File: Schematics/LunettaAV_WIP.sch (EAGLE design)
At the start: 50 parts, among them IC1 TLC339P, IC2 7805T, IC3 4046N, IC4 4040N, IC5 4017N, IC6 4051N, IC7 4094N, IC8 4046N, IC9 40106N, U1 LM358

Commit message: schematic updates
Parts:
- added C2: .1uF, capacitor-wima:C2.5/2
- added R23: LDR, rcl:R-EU_0204/2V
- added VR4: 100K, MusicThingModular:9MM_SNAP-IN_POT_
- R21: value (none) -> 10K
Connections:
- removed net MELODYBUFF: D1.C, VR3.E
- new net N$10: IC9B.O, IC9C.I
- new net N$12: C2.1, IC9A.I, R23.2, VR4.S
- new net N$9: IC9A.O, IC9B.I, R23.1, VR4.A
- net AUDIORATE: now also IC9C.O
- net GND: now also C2.2, IC9D.I, IC9E.I, IC9F.I
- net MELODYOUT: now also D1.C, VR3.E
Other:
- moved on the sheet: IC9A, IC9B, IC9C, IC9D, IC9E, IC9F, IC9P, JP6

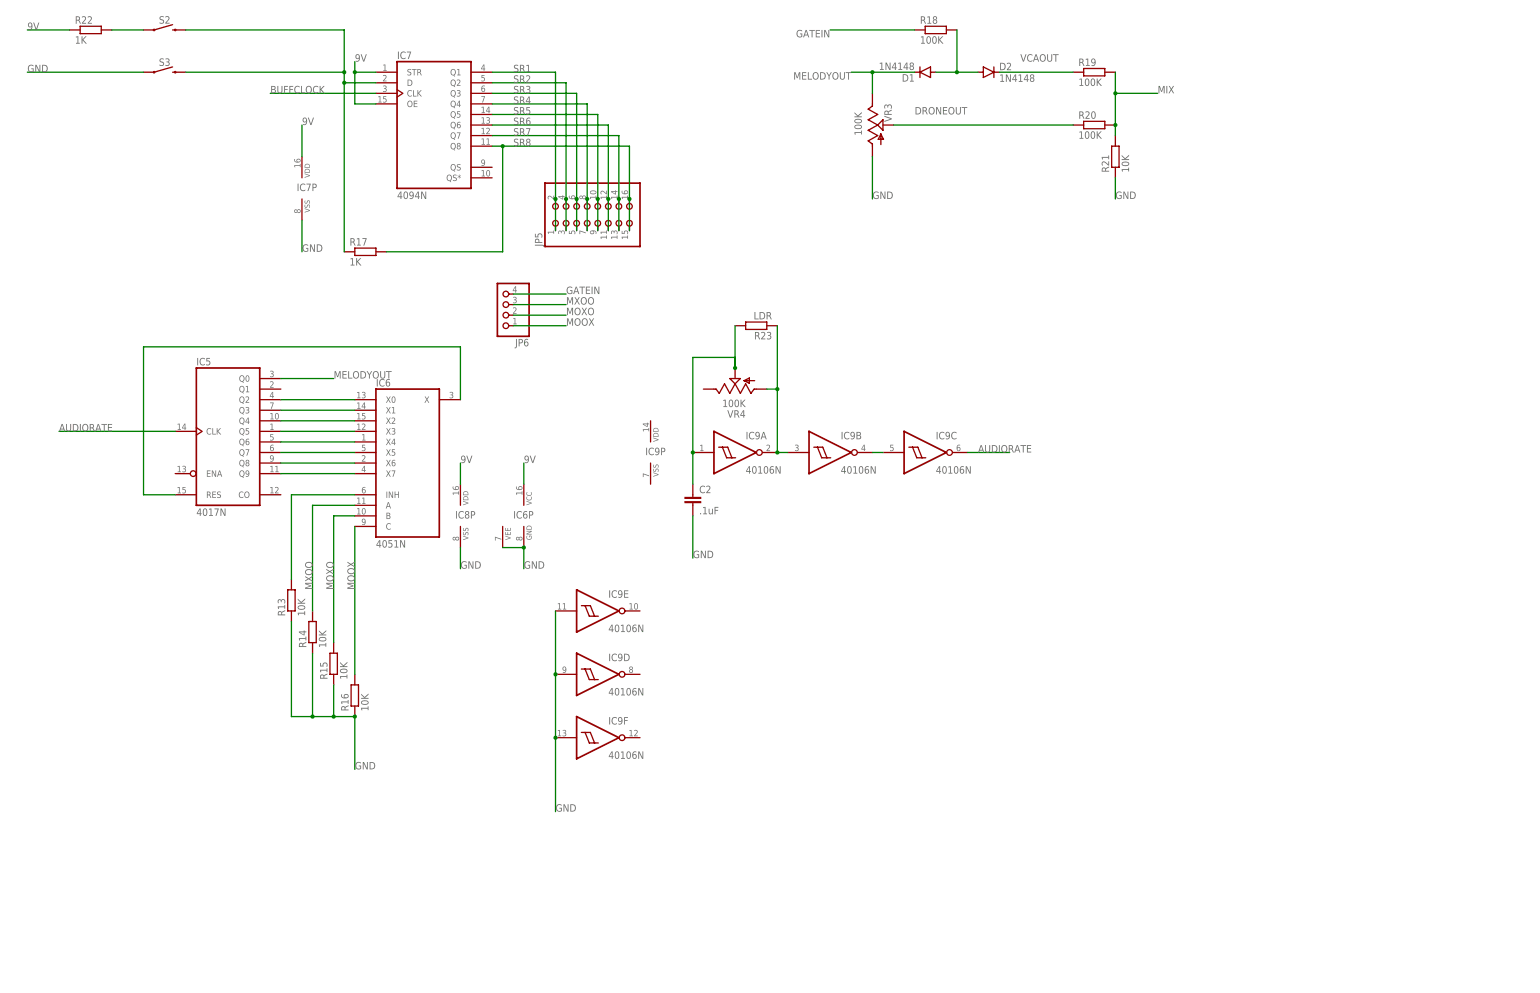
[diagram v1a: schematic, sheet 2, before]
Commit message: more visuals and functions updated
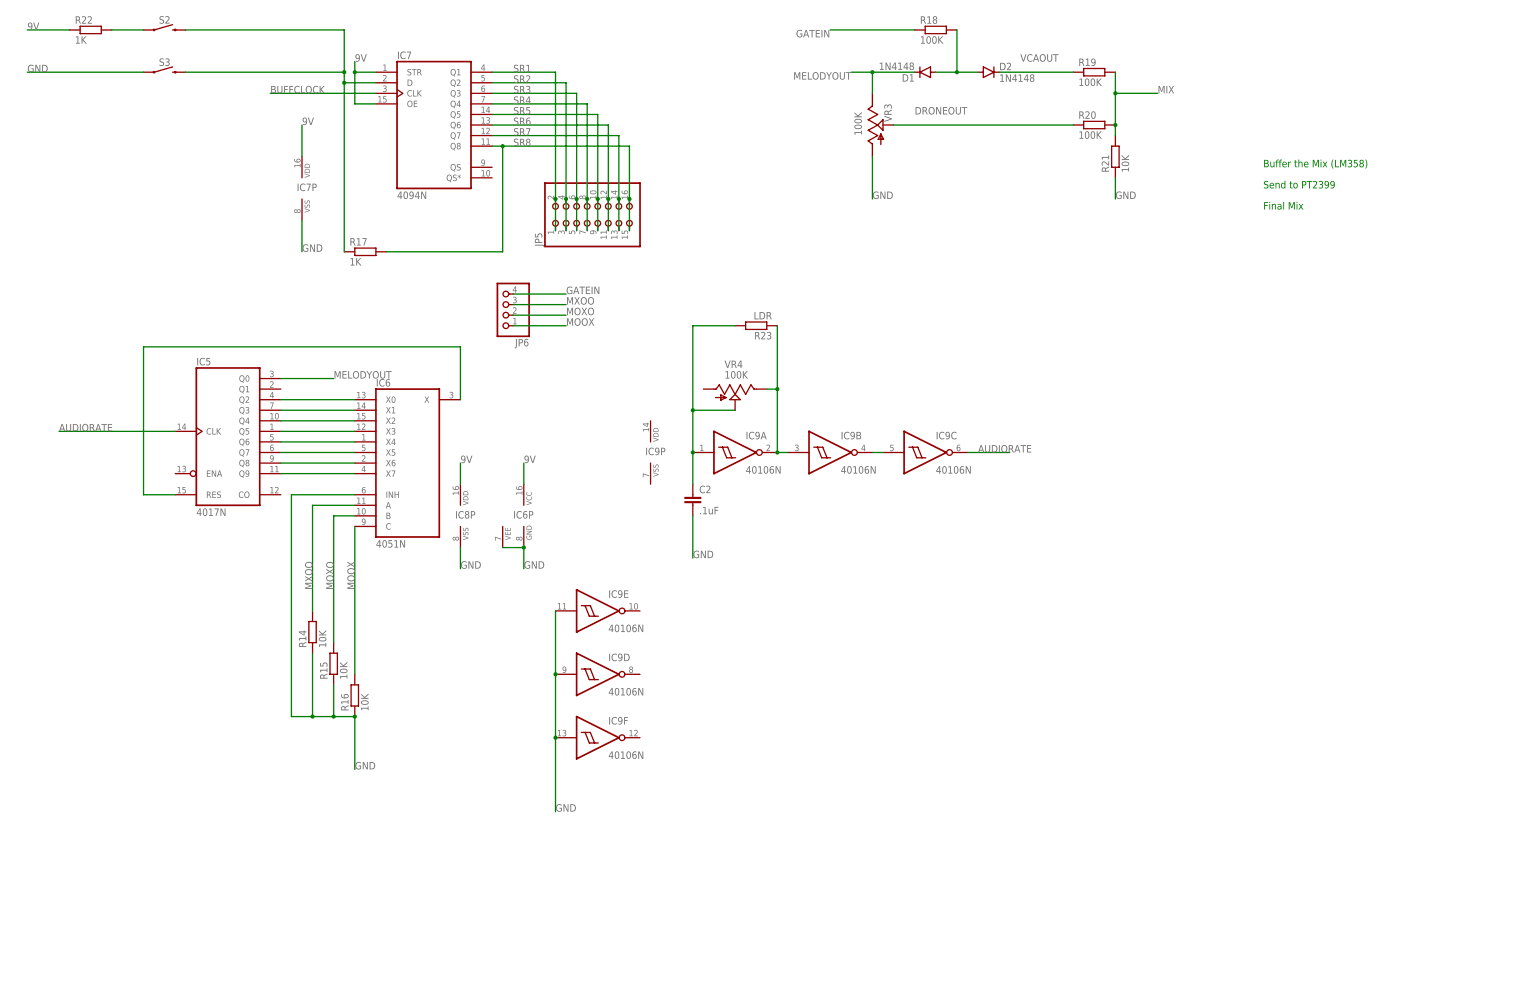
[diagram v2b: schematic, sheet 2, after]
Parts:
- removed R13: 10K, MusicThingModular:RESISTOR7MM
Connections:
- removed net N$11 (its old number): IC6A.INH, R13.2
- net GND: now also IC6A.INH; no longer R13.1
- net N$9: now also VR4.E; no longer VR4.A
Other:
- note added: "Buffer the Mix (LM358)"
- note added: "Final Mix"
- note added: "Send to PT2399"
- moved on the sheet: VR4
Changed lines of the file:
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@@
 <part name="R21" library="MusicThingModular" deviceset="RESISTOR" device="7MM" value="10K"/>
 <part name="R17" library="MusicThingModular" deviceset="RESISTOR" device="7MM" value="1K"/>
-<part name="R13" library="MusicThingModular" deviceset="RESISTOR" device="7MM" value="10K"/>
 <part name="R14" library="MusicThingModular" deviceset="RESISTOR" device="7MM" value="10K"/>
 <part name="R15" library="MusicThingModular" deviceset="RESISTOR" device="7MM" value="10K"/>
@@
 <sheet>
 <plain>
+<text x="314.96" y="-116.84" size="1.778" layer="91">Buffer the Mix (LM358)</text>
+<text x="314.96" y="-121.92" size="1.778" layer="91">Send to PT2399</text>
+<text x="314.96" y="-127" size="1.778" layer="91">Final Mix</text>
 </plain>
 <instances>
@@
 <attribute name="VALUE" x="95.25" y="-140.462" size="1.778" layer="96"/>
 </instance>
-<instance part="R13" gate="G$1" x="81.28" y="-220.98" smashed="yes" rot="R90">
-<attribute name="NAME" x="79.7814" y="-224.79" size="1.778" layer="95" rot="R90"/>
-<attribute name="VALUE" x="84.582" y="-224.79" size="1.778" layer="96" rot="R90"/>
-</instance>
 <instance part="R14" gate="G$1" x="86.36" y="-228.6" smashed="yes" rot="R90">
 <attribute name="NAME" x="84.8614" y="-232.41" size="1.778" layer="95" rot="R90"/>
@@
 <attribute name="VALUE" x="29.21" y="-87.122" size="1.778" layer="96"/>
 </instance>
-<instance part="VR4" gate="G$1" x="187.96" y="-170.18" smashed="yes" rot="R90">
-<attribute name="NAME" x="190.5" y="-175.26" size="1.778" layer="95" rot="R180"/>
-<attribute name="VALUE" x="190.5" y="-172.72" size="1.778" layer="96" rot="R180"/>
+<instance part="VR4" gate="G$1" x="187.96" y="-170.18" smashed="yes" rot="R270">
+<attribute name="NAME" x="185.42" y="-165.1" size="1.778" layer="95"/>
+<attribute name="VALUE" x="185.42" y="-167.64" size="1.778" layer="96"/>
 </instance>
 <instance part="C2" gate="G$1" x="177.8" y="-195.58" smashed="yes">
@@
 </segment>
 <segment>
-<pinref part="R13" gate="G$1" pin="1"/>
-<wire x1="81.28" y1="-226.06" x2="81.28" y2="-248.92" width="0.1524" layer="91"/>
 <pinref part="R16" gate="G$1" pin="1"/>
 <wire x1="81.28" y1="-248.92" x2="86.36" y2="-248.92" width="0.1524" layer="91"/>
@@
 <junction x="86.36" y="-248.92"/>
 <label x="96.52" y="-261.62" size="1.778" layer="95"/>
+<pinref part="IC6" gate="A" pin="INH"/>
+<wire x1="96.52" y1="-195.58" x2="81.28" y2="-195.58" width="0.1524" layer="91"/>
+<wire x1="81.28" y1="-195.58" x2="81.28" y2="-248.92" width="0.1524" layer="91"/>
 </segment>
 <segment>
@@
 </segment>
 </net>
-<net name="N$11" class="0">
-<segment>
-<pinref part="IC6" gate="A" pin="INH"/>
-<pinref part="R13" gate="G$1" pin="2"/>
-<wire x1="96.52" y1="-195.58" x2="81.28" y2="-195.58" width="0.1524" layer="91"/>
-<wire x1="81.28" y1="-195.58" x2="81.28" y2="-215.9" width="0.1524" layer="91"/>
-</segment>
-</net>
 <net name="N$8" class="0">
 <segment>
@@
 <pinref part="IC9" gate="B" pin="I"/>
 <wire x1="198.12" y1="-185.42" x2="200.66" y2="-185.42" width="0.1524" layer="91"/>
-<wire x1="198.12" y1="-185.42" x2="198.12" y2="-170.18" width="0.1524" layer="91"/>
 <junction x="198.12" y="-185.42"/>
-<pinref part="VR4" gate="G$1" pin="A"/>
-<wire x1="198.12" y1="-170.18" x2="195.58" y2="-170.18" width="0.1524" layer="91"/>
 <pinref part="R23" gate="G$1" pin="1"/>
 <wire x1="198.12" y1="-154.94" x2="198.12" y2="-170.18" width="0.1524" layer="91"/>
+<pinref part="VR4" gate="G$1" pin="E"/>
+<wire x1="198.12" y1="-170.18" x2="198.12" y2="-185.42" width="0.1524" layer="91"/>
+<wire x1="195.58" y1="-170.18" x2="198.12" y2="-170.18" width="0.1524" layer="91"/>
 <junction x="198.12" y="-170.18"/>
 </segment>
@@
 </segment>
 </net>
-<net name="N$12" class="0">
-<segment>
+<net name="N$11" class="0">
+<segment>
+<pinref part="C2" gate="G$1" pin="1"/>
 <pinref part="IC9" gate="A" pin="I"/>
 <wire x1="177.8" y1="-185.42" x2="177.8" y2="-193.04" width="0.1524" layer="91"/>
-<pinref part="C2" gate="G$1" pin="1"/>
 <pinref part="VR4" gate="G$1" pin="S"/>
-<wire x1="187.96" y1="-165.1" x2="187.96" y2="-162.56" width="0.1524" layer="91"/>
-<wire x1="187.96" y1="-162.56" x2="177.8" y2="-162.56" width="0.1524" layer="91"/>
-<wire x1="177.8" y1="-162.56" x2="177.8" y2="-185.42" width="0.1524" layer="91"/>
+<wire x1="187.96" y1="-175.26" x2="177.8" y2="-175.26" width="0.1524" layer="91"/>
+<wire x1="177.8" y1="-175.26" x2="177.8" y2="-185.42" width="0.1524" layer="91"/>
 <junction x="177.8" y="-185.42"/>
 <pinref part="R23" gate="G$1" pin="2"/>
-<wire x1="187.96" y1="-154.94" x2="187.96" y2="-165.1" width="0.1524" layer="91"/>
-<junction x="187.96" y="-165.1"/>
-</segment>
-</net>
+<wire x1="187.96" y1="-154.94" x2="177.8" y2="-154.94" width="0.1524" layer="91"/>
+<wire x1="177.8" y1="-154.94" x2="177.8" y2="-175.26" width="0.1524" layer="91"/>
+<junction x="177.8" y="-175.26"/>
+</segment>
+</net>

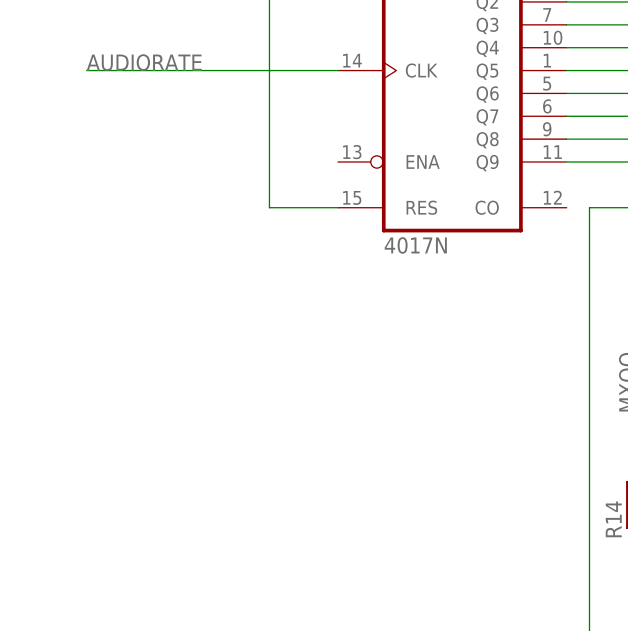
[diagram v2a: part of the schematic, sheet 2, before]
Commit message: fix 4017 schematics
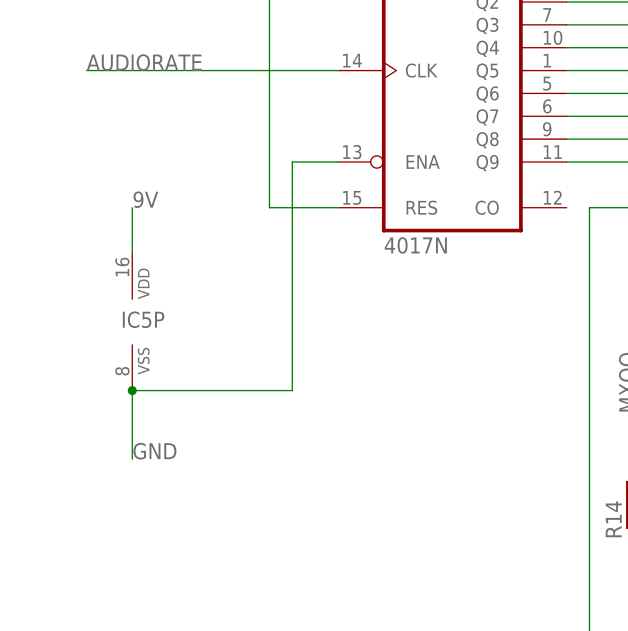
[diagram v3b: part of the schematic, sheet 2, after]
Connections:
- net 9V: now also IC5P.VDD
- net GND: now also IC5A.ENA, IC5P.VSS
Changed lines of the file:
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@@
 <attribute name="VALUE" x="196.85" y="-151.638" size="1.778" layer="96" rot="R180"/>
+</instance>
+<instance part="IC5" gate="P" x="30.48" y="-208.28" smashed="yes">
+<attribute name="NAME" x="29.21" y="-208.915" size="1.778" layer="95"/>
 </instance>
 </instances>
@@
 <wire x1="27.94" y1="-83.82" x2="17.78" y2="-83.82" width="0.1524" layer="91"/>
 <label x="17.78" y="-83.82" size="1.778" layer="95"/>
+</segment>
+<segment>
+<pinref part="IC5" gate="P" pin="VDD"/>
+<wire x1="30.48" y1="-200.66" x2="30.48" y2="-195.58" width="0.1524" layer="91"/>
+<label x="30.48" y="-195.58" size="1.778" layer="95"/>
 </segment>
 </net>
@@
 <label x="144.78" y="-271.78" size="1.778" layer="95"/>
 </segment>
+<segment>
+<pinref part="IC5" gate="P" pin="VSS"/>
+<wire x1="30.48" y1="-215.9" x2="30.48" y2="-223.52" width="0.1524" layer="91"/>
+<label x="30.48" y="-223.52" size="1.778" layer="95"/>
+<pinref part="IC5" gate="A" pin="ENA"/>
+<wire x1="53.34" y1="-190.5" x2="48.26" y2="-190.5" width="0.1524" layer="91"/>
+<wire x1="48.26" y1="-190.5" x2="48.26" y2="-215.9" width="0.1524" layer="91"/>
+<wire x1="48.26" y1="-215.9" x2="30.48" y2="-215.9" width="0.1524" layer="91"/>
+<junction x="30.48" y="-215.9"/>
+</segment>
 </net>

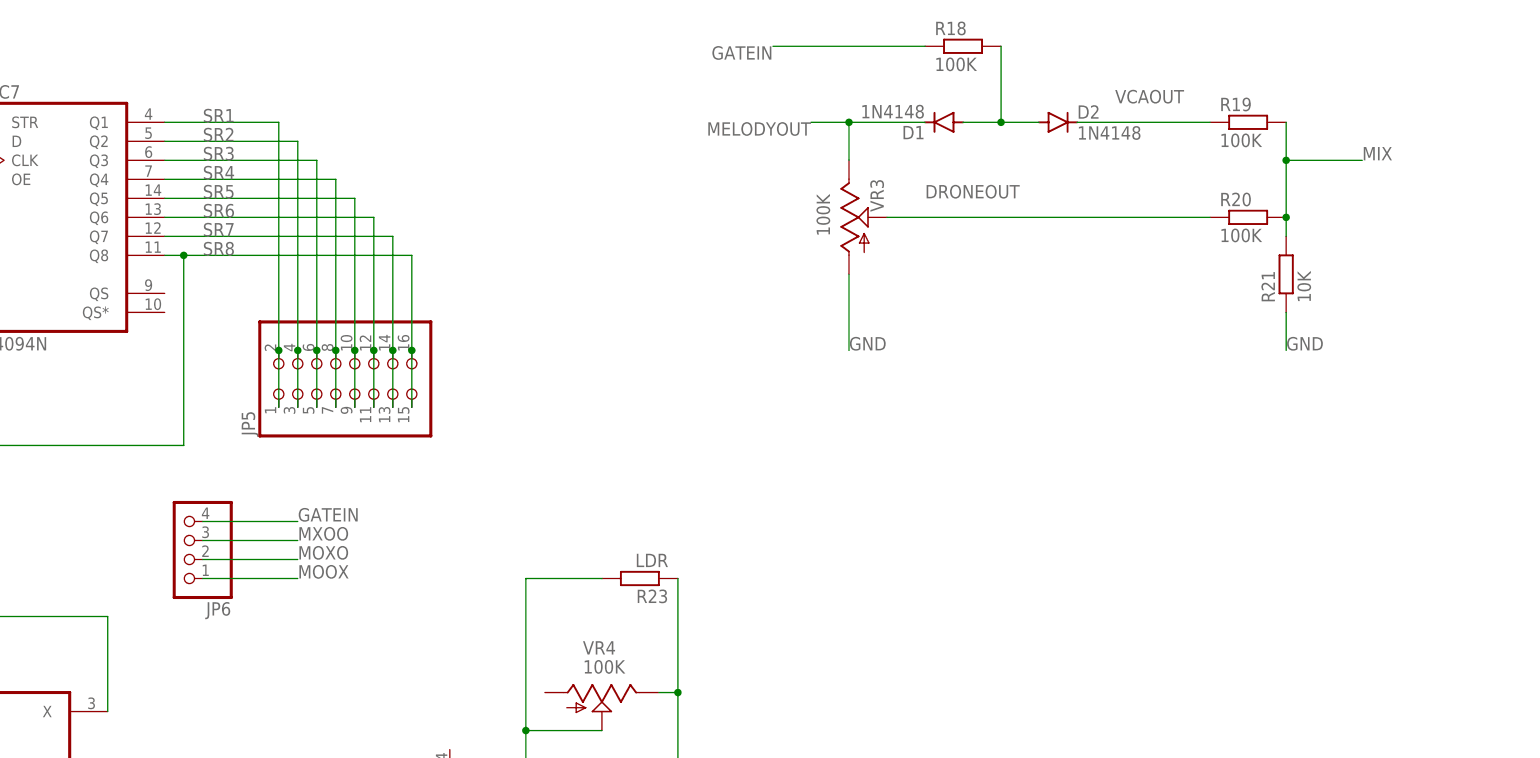
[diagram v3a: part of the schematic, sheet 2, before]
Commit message: change melody out config and buffer the out for later stage
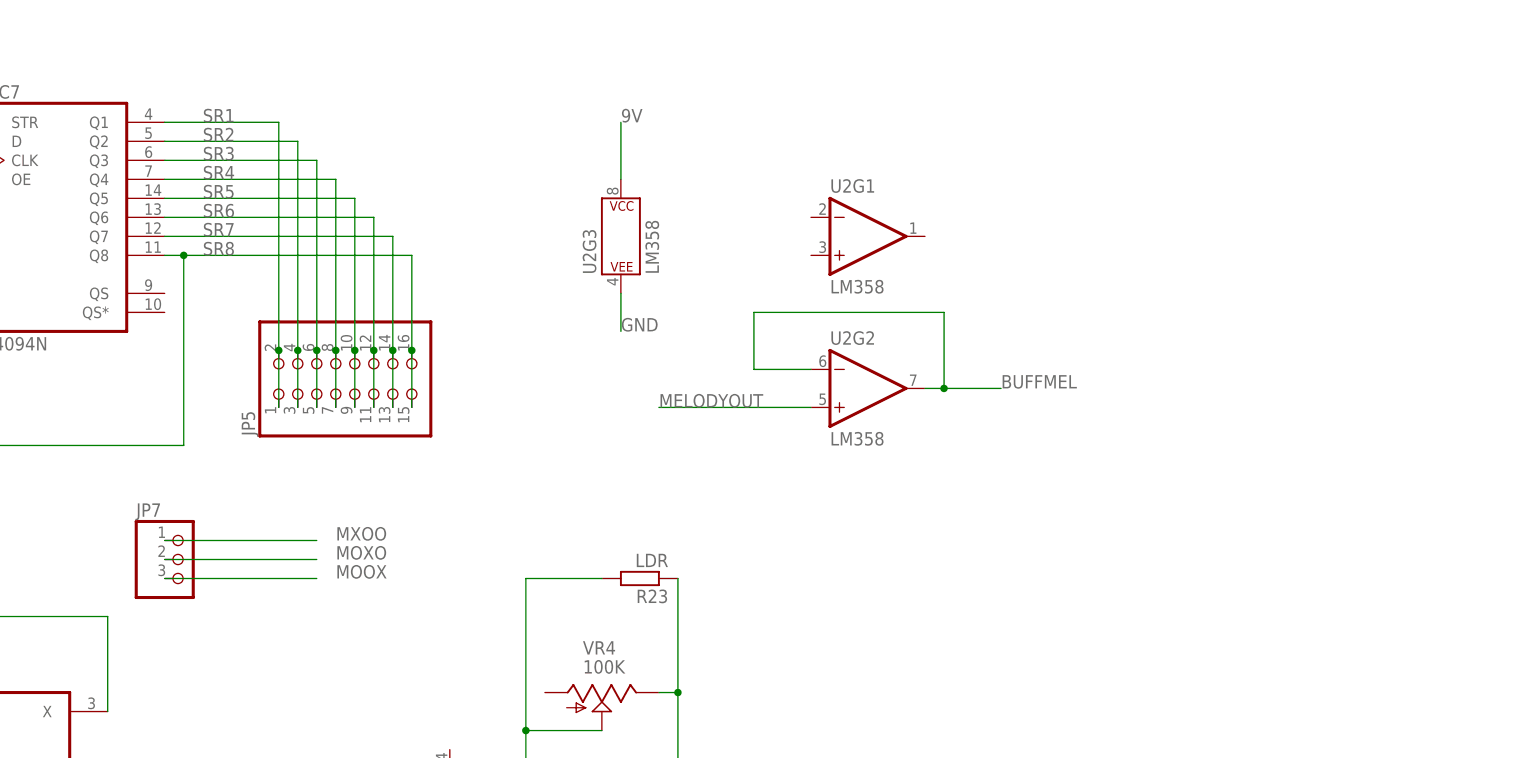
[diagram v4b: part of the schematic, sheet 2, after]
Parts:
- removed D1, D2: 1N4148, diode:1N4148DO35-10
- removed JP6: (no value), pinhead:PINHD-1X4
- removed R18, R19, R20: 100K, MusicThingModular:RESISTOR7MM
- removed R21: 10K, MusicThingModular:RESISTOR7MM
- removed VR3: 100K, MusicThingModular:9MM_SNAP-IN_POT_
- added JP7: (no value), pinhead:PINHD-1X3
- added U2: LM358, SparkFun-IC-Amplifiers:LM358
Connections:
- removed net DRONEOUT: R20.1, VR3.S
- removed net GATEIN: JP6.4, R18.1
- removed net MIX: R19.2, R20.2, R21.2
- removed net N$7: D1.A, D2.A, R18.2
- removed net VCAOUT: D2.C, R19.1
- new net BUFFMEL: U2G2.-IN, U2G2.OUT
- net 9V: now also U2G3.P$V+
- net GND: now also U2G3.P$V-; no longer R21.1, VR3.A
- net MELODYOUT: now also U2G2.+IN; no longer D1.C, VR3.E
- net MOOX: now also JP7.3; no longer JP6.1
- net MOXO: now also JP7.2; no longer JP6.2
- net MXOO: now also JP7.1; no longer JP6.3

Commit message: PT2399 init + screen changed
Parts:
- removed DISP$1, DISP$2: DISPLAY-OLED-128X64-I2C, diy-modules:DISPLAY-OLED-128X64-I2C
- added C10, C8, C9: 10uF, SparkFun-Capacitors:10UF-POLAR-RADIAL-2.5MM-25V-20%
- added C11: 47uF, SparkFun-Capacitors:10UF-POLAR-RADIAL-2.5MM-25V-20%
- added C12, C13, C4, C5, C6, C7: 0.1uF, SparkFun-Capacitors:0.1UF-KIT-EZ-50V-20%
- added C3: 100uF, SparkFun-Capacitors:100UF-POLAR-RADIAL-2.5MM-25V-20%
- added DD1: PT2399, ic-princeton-technologies:PT2399
- added IC10: (no value), v-reg:78XXS
- added J1: POWER_JACKPOWER_JACK_SLOT, SparkFun-Connectors:POWER_JACKPOWER_JACK_SLOT
- added R13: (no value), MusicThingModular:RESISTOR7MM
- added R18: 10k, MusicThingModular:RESISTOR7MM
- added R19: 100k, MusicThingModular:RESISTOR7MM
- added U$1, U$2: OLED_0.96_I2C, tft_1_8_1_44_oled_0_96:OLED_0.96_I2C
- added VR3: (no value), MusicThingModular:9MM_SNAP-IN_POT_
- C1: value 1uF -> 10nF
- IC2: value 7805T -> 7805; device linear:7805T -> v-reg:78XXS
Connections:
- new net DCIN: C10.+, IC10.IN, J1.PWR
- new net N$12: C6.1, DD1.10
- new net N$13: C7.2, DD1.11
- new net N$14: C7.1, DD1.12
- new net N$15: DD1.6, R13.2
- new net N$16: C11.+, DD1.2
- new net N$17: C5.2, DD1.7
- new net N$18: C4.1, DD1.8
- new net N$29: DD1.16, R18.1, R19.2
- new net N$30: DD1.15, R18.2
- new net N$7: C6.2, DD1.9
- net 3V3: now also C12.1, C13.1, U$1.VCC, U$2.VCC; no longer DISP$1.VCC, DISP$2.VCC
- net 5V: now also C3.+, C9.+, DD1.1, IC2.OUT; no longer IC2.VO
- net 9V: now also C8.+, IC10.OUT, IC2.IN; no longer IC2.VI
- net BUFFMEL: now also R19.1
- net GND: now also C10.-, C11.-, C12.2, C13.2, C3.-, C4.2, C5.1, C8.-, C9.-, DD1.3, DD1.4, IC10.GND, J1.GND, U$1.GND, U$2.GND; no longer DISP$1.GND, DISP$2.GND
- net N$3: now also U$1.SCL, U$2.SCL; no longer DISP$1.SCL, DISP$2.SCL
- net N$4: now also U$1.SDA, U$2.SDA; no longer DISP$1.SDA, DISP$2.SDA
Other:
- moved on the sheet: C2, IC9A, IC9B, IC9C, IC9D, IC9E, IC9F, IC9P, R23, U2G1, U2G2, U2G3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
